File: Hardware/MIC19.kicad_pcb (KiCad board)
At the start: 2 copper layers, 85 parts, among them J1 Screw_Terminal_01x02, J2 Screw_Terminal_01x03, J401 USART, J601 RJ45, J602 RJ45, K1 coil: 12VDC, contact: 125V/10A, Q1 Q_NPN_BEC, U1 4N25, U201 MCP2551-I/SN, U202 MCP2515-xSO, U401 ATMEGA328P-PU, U501 LM7805, Y201 16MHz, Y401 16MHz

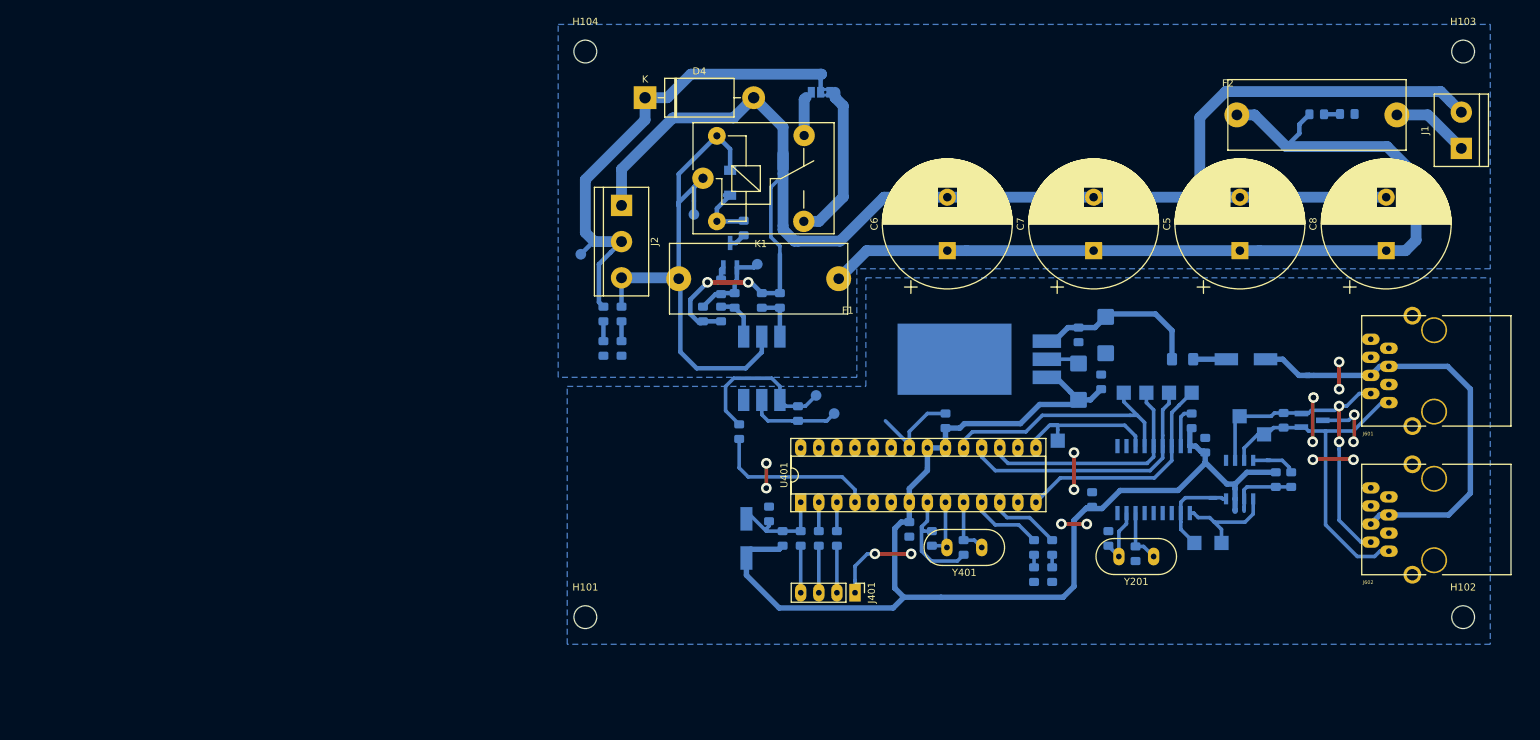
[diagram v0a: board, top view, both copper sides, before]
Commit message: Atualização do MIC19
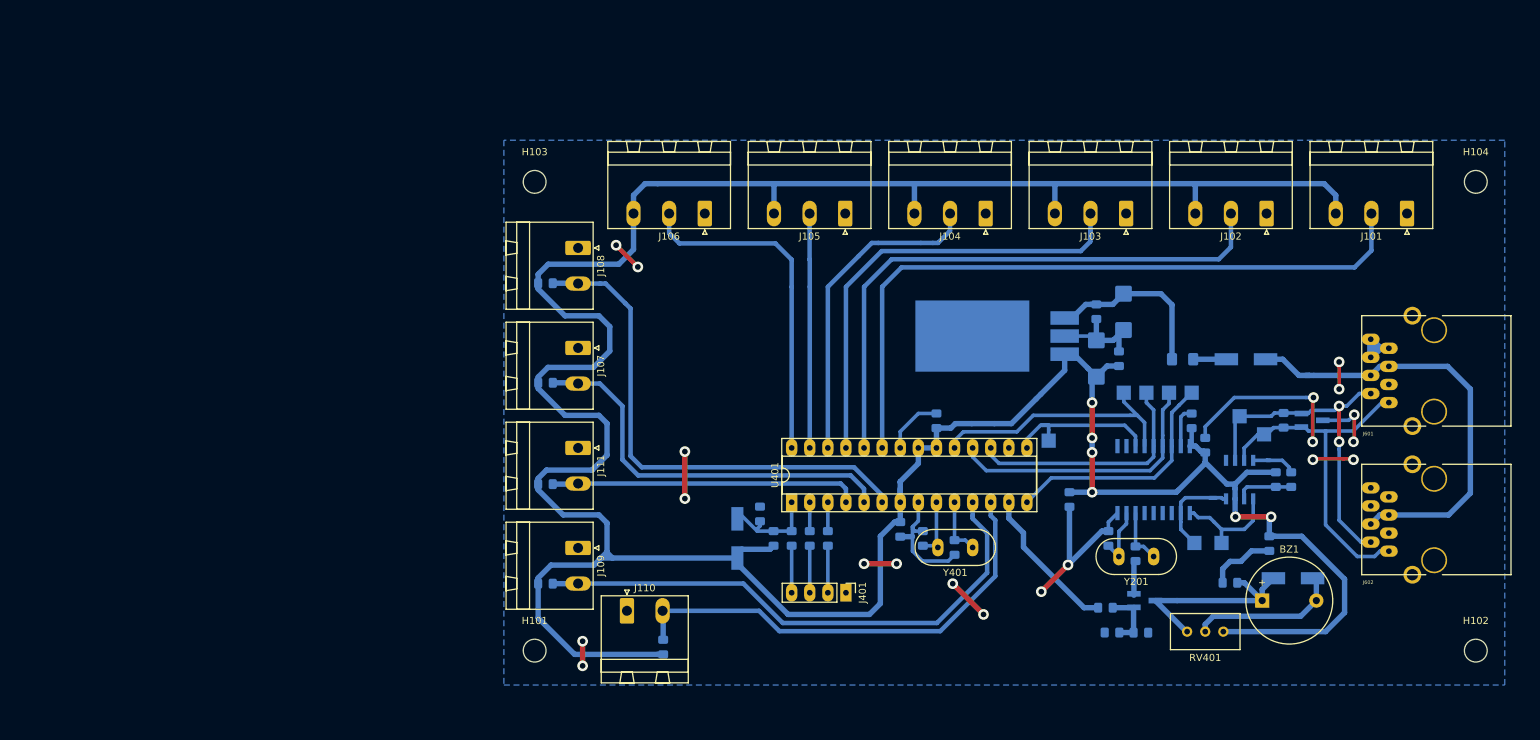
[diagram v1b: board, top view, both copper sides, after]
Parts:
- removed C1, C3, C4: 100n, Capacitor_SMD:C_0805_2012Metric_Pad1.15x1.40mm_HandSolder
- removed C2: 1n, Capacitor_SMD:C_0805_2012Metric_Pad1.15x1.40mm_HandSolder
- removed C5, C6, C7, C8: 4700u 35V, Capacitor_THT:CP_Radial_D18.0mm_P7.50mm
- removed D1, D5: G3mm, LED_SMD:LED_0805_2012Metric_Pad1.15x1.40mm_HandSolder
- removed D2: LL4148, Diode_SMD:D_MiniMELF
- removed D3: R3mm, LED_SMD:LED_0805_2012Metric_Pad1.15x1.40mm_HandSolder
- removed D4: MUR460, Diode_THT:D_DO-201AD_P15.24mm_Horizontal
- removed F1: 3A, KicadZeniteSolarLibrary18:Fuse_Holder_5x20
- removed F2: 10A, KicadZeniteSolarLibrary18:Fuse_Holder_5x20
- removed J1: Screw_Terminal_01x02, TerminalBlock:TerminalBlock_bornier-2_P5.08mm
- removed J2: Screw_Terminal_01x03, TerminalBlock:TerminalBlock_bornier-3_P5.08mm
- removed JP1: SolderJumper_3_Bridged12, Jumper:SolderJumper-3_P1.3mm_Bridged2Bar12_Pad1.0x1.5mm_NumberLabels
- removed K1: coil: 12VDC, contact: 125V/10A, Relay_THT:Relay_SPDT_SANYOU_SRD_Series_Form_C
- removed Q1: Q_NPN_BEC, Package_TO_SOT_SMD:TSOT-23_HandSoldering
- removed R1: 330R, Resistor_SMD:R_0805_2012Metric_Pad1.15x1.40mm_HandSolder
- removed R2: NC, Resistor_SMD:R_0805_2012Metric_Pad1.15x1.40mm_HandSolder
- removed R3: 1k2, Resistor_SMD:R_0805_2012Metric_Pad1.15x1.40mm_HandSolder
- removed R4, R7, R8: 1k, Resistor_SMD:R_0805_2012Metric_Pad1.15x1.40mm_HandSolder
- removed R5: 10k, Resistor_SMD:R_0805_2012Metric_Pad1.15x1.40mm_HandSolder
- removed R6: 120R, Resistor_SMD:R_0805_2012Metric_Pad1.15x1.40mm_HandSolder
- removed TP1: A1, TestPoint:TestPoint_Pad_D1.5mm
- removed TP2: K1, TestPoint:TestPoint_Pad_D1.5mm
- removed TP3: 12V, TestPoint:TestPoint_Pad_D1.5mm
- removed TP4: B1, TestPoint:TestPoint_Pad_D1.5mm
- removed TP5: OUT1, TestPoint:TestPoint_Pad_D1.5mm
- removed U1: 4N25, Package_DIP:DIP-6_W8.89mm_SMDSocket_LongPads
- added BZ1: Buzzer, Buzzer_Beeper:Buzzer_12x9.5RM7.6, F.Cu at (175.0, 121.5)
- added C407: 100nF, Capacitor_SMD:C_0805_2012Metric_Pad1.15x1.40mm_HandSolder, B.Cu at (158.0, 126.0)
- added J101: ENGINE_VEL, Connector_Phoenix_MSTB:PhoenixContact_MSTBA_2,5_3-G_1x03_P5.00mm_Horizontal, F.Cu at (195.3, 67.2)
- added J102: ENGINE_ACEL, Connector_Phoenix_MSTB:PhoenixContact_MSTBA_2,5_3-G_1x03_P5.00mm_Horizontal, F.Cu at (175.6, 67.2)
- added J103: MPPT_POT, Connector_Phoenix_MSTB:PhoenixContact_MSTBA_2,5_3-G_1x03_P5.00mm_Horizontal, F.Cu at (155.9, 67.2)
- added J104: SW_PUMP1_ON, Connector_Phoenix_MSTB:PhoenixContact_MSTBA_2,5_3-G_1x03_P5.00mm_Horizontal, F.Cu at (136.2, 67.2)
- added J105: SW_PUMP2_ON, Connector_Phoenix_MSTB:PhoenixContact_MSTBA_2,5_3-G_1x03_P5.00mm_Horizontal, F.Cu at (116.5, 67.2)
- added J106: SW_PUMP3_ON, Connector_Phoenix_MSTB:PhoenixContact_MSTBA_2,5_3-G_1x03_P5.00mm_Horizontal, F.Cu at (96.8, 67.2)
- added J107: SW_BOAT_ON, Connector_Phoenix_MSTB:PhoenixContact_MSTBA_2,5_2-G_1x02_P5.00mm_Horizontal, F.Cu at (79.0, 86.0)
- added J108: SW_ENGINE_ON, Connector_Phoenix_MSTB:PhoenixContact_MSTBA_2,5_2-G_1x02_P5.00mm_Horizontal, F.Cu at (79.0, 72.0)
- added J109: SW_MPPT_ON, Connector_Phoenix_MSTB:PhoenixContact_MSTBA_2,5_2-G_1x02_P5.00mm_Horizontal, F.Cu at (79.0, 114.1)
- added J110: SW_DMS, Connector_Phoenix_MSTB:PhoenixContact_MSTBA_2,5_2-G_1x02_P5.00mm_Horizontal, F.Cu at (85.9, 122.9)
- added J111: SW_EMERGENCIA, Connector_Phoenix_MSTB:PhoenixContact_MSTBA_2,5_2-G_1x02_P5.00mm_Horizontal, F.Cu at (79.0, 100.1)
- added Q101: BCV27, Package_TO_SOT_SMD:SOT-23_Handsoldering, B.Cu at (158.5, 121.5)
- added R101: 1k, Resistor_SMD:R_0805_2012Metric_Pad1.15x1.40mm_HandSolder, B.Cu at (74.4, 90.9)
- added R102: 1k, Resistor_SMD:R_0805_2012Metric_Pad1.15x1.40mm_HandSolder, B.Cu at (74.4, 77.0)
- added R103: 1k, Resistor_SMD:R_0805_2012Metric_Pad1.15x1.40mm_HandSolder, B.Cu at (74.4, 119.1)
- added R104: 1k, Resistor_SMD:R_0805_2012Metric_Pad1.15x1.40mm_HandSolder, B.Cu at (90.9, 128.0)
- added R105: 1k, Resistor_SMD:R_0805_2012Metric_Pad1.15x1.40mm_HandSolder, B.Cu at (74.4, 105.2)
- added R406: 330, Resistor_SMD:R_0805_2012Metric_Pad1.15x1.40mm_HandSolder, B.Cu at (176.0, 113.5)
- added RV401: 1K, Potentiometer_THT:Potentiometer_Bourns_3296W_Vertical, F.Cu at (164.5, 125.9)
- D402: value LED_RED -> BYD77; footprint LED_SMD:LED_0805_2012Metric_Pad1.15x1.40mm_HandSolder -> Diode_SMD:D_MiniMELF_Handsoldering
- R404, R405: value 1k -> 100R
- moved H103 131.6 mm to (72.9, 62.7)
- moved H104 126.3 mm to (205.0, 62.7)
- moved D402 33.8 mm to (179.3, 118.4), turned to 180 degrees
- moved D403 27.5 mm to (170.5, 119.0), turned to 180 degrees
- moved R405 16.2 mm to (153.9, 126.0), turned to 0 degrees
- moved R404 11.3 mm to (153.0, 122.5), turned to 0 degrees
- moved H101 8.52 mm to (72.9, 128.5)
- moved H102 5.02 mm to (205.0, 128.5)
- moved C501 4.10 mm to (155.5, 81.0)
- moved C502 4.10 mm to (151.7, 81.0)
- moved C503 4.10 mm to (154.9, 87.6)
- moved C504 4.10 mm to (151.7, 87.5)
- moved U501 4.10 mm to (146.0, 81.8)
- moved C201 3.17 mm to (148.0, 107.3), turned to 270 degrees
- moved C401 1.27 mm to (129.3, 96.3)
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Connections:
- D402 pad 1: GND -> Net-(BZ1-Pad2)
- D402 pad 2: Net-(D402-Pad2) -> Net-(BZ1-Pad1)
- D403 pad 1: GND -> Net-(BZ1-Pad1)
- R404 pad 1: /MCU/LED2 -> Net-(R404-Pad1)
- R404 pad 2: Net-(D402-Pad2) -> Net-(C407-Pad2)
- R405 pad 1: /MCU/LED1 -> GND
- R405 pad 2: Net-(D403-Pad2) -> Net-(C407-Pad2)
- U401 pad 11: /MCU/LED1 -> /Conectores/SW_MPPT_ON
- U401 pad 12: /MCU/LED2 -> /Conectores/SW_DMS
- U401 pad 13: Net-(U401-Pad13) -> Net-(R404-Pad1)
- U401 pad 23: Net-(U401-Pad23) -> /Conectores/ENGINE_VEL
- U401 pad 24: Net-(U401-Pad24) -> /Conectores/ENGINE_ACEL
- U401 pad 25: Net-(U401-Pad25) -> /Conectores/MPPT_POT
- U401 pad 26: Net-(U401-Pad26) -> /Conectores/SW_PUMP1_ON
- U401 pad 27: Net-(U401-Pad27) -> /Conectores/SW_PUMP2_ON
- U401 pad 28: Net-(U401-Pad28) -> /Conectores/SW_PUMP3_ON
- U401 pad 4: /MCU/ON_OFF_PUMP -> /Conectores/SW_EMERGENCIA
- U401 pad 5: Net-(U401-Pad5) -> /Conectores/SW_BOAT_ON
- U401 pad 6: Net-(U401-Pad6) -> /Conectores/SW_ENGINE_ON
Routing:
- net +5V: track 170.6 -> 475.8 mm, vias 0 -> 6
- net GNDPWR: track 239.1 -> 0.00 mm, vias 2 -> 0
- net +12V: track 126.9 -> 0.00 mm
- net /Conectores/ENGINE_VEL: track 0.00 -> 98.6 mm
- net /Conectores/ENGINE_ACEL: track 0.00 -> 81.7 mm
- net /pump_driver/Level_sensor: track 77.1 -> 0.00 mm
- net /Conectores/SW_MPPT_ON: track 0.00 -> 76.9 mm
- net /Conectores/SW_ENGINE_ON: track 0.00 -> 72.1 mm
- net /pump_driver/+Pump: track 69.5 -> 0.00 mm
- net /Conectores/SW_DMS: track 0.00 -> 65.8 mm
- net /Conectores/MPPT_POT: track 0.00 -> 64.3 mm
- net /Conectores/SW_BOAT_ON: track 0.00 -> 57.4 mm
- net /Conectores/SW_PUMP3_ON: track 0.00 -> 48.7 mm
- net GND: track 108.8 -> 156.5 mm, vias 16 -> 20
- net /Conectores/SW_PUMP1_ON: track 0.00 -> 45.5 mm
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- removed copper zone on B.Cu, net GNDPWR

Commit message: Formato da placa modificado
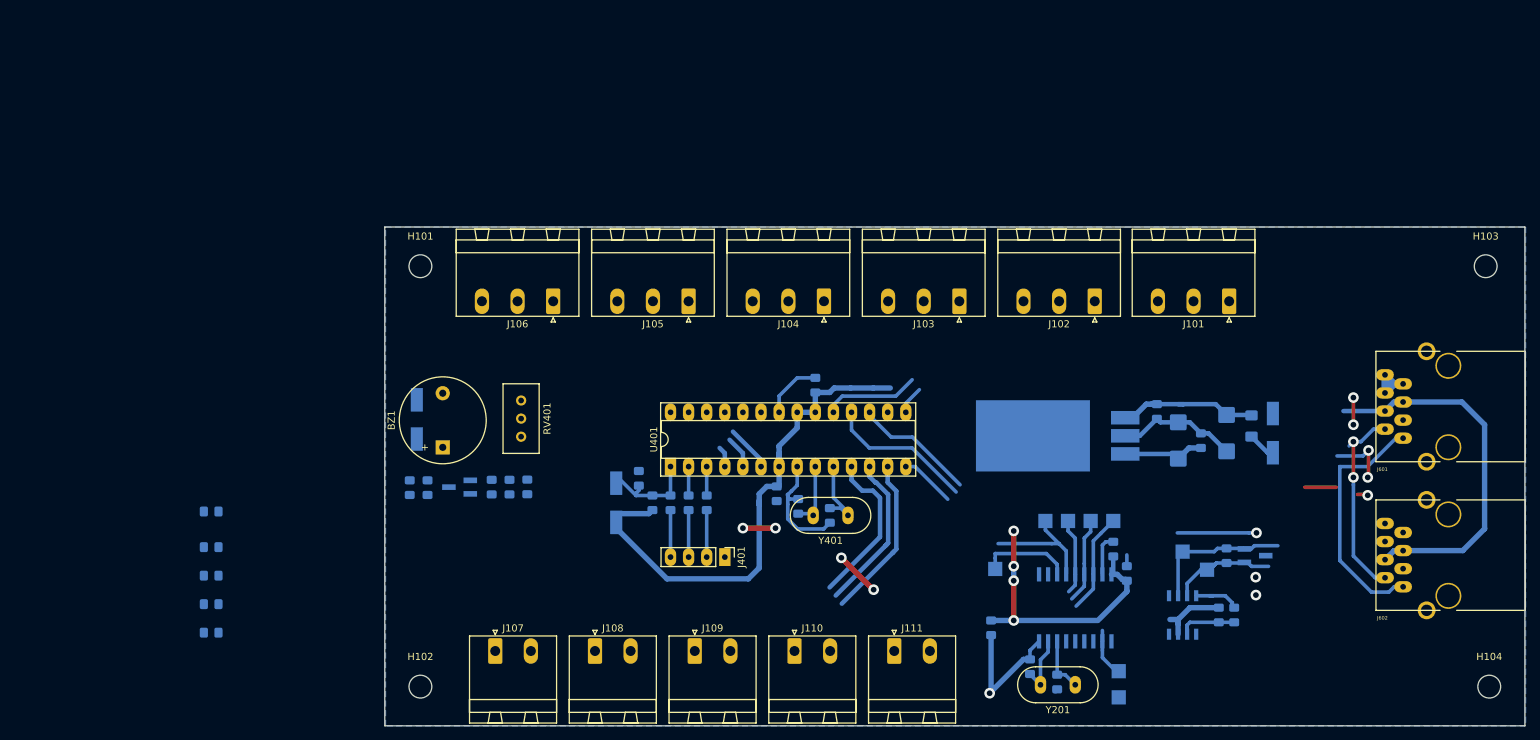
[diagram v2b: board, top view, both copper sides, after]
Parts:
- moved H102 148.2 mm to (56.9, 133.6)
- moved H103 134.0 mm to (206.4, 74.6)
- moved D402 125.0 mm to (56.4, 96.1), turned to 270 degrees
- moved R406 118.4 mm to (57.9, 105.7)
- moved BZ1 117.0 mm to (60.0, 100.0), turned to 90 degrees
- moved D403 115.9 mm to (55.4, 105.7), turned to 270 degrees
- moved Q101 97.4 mm to (62.4, 105.6), turned to 180 degrees
- moved RV401 97.4 mm to (71.0, 98.5), turned to 270 degrees
- moved C407 93.4 mm to (66.9, 105.6), turned to 90 degrees
- moved R405 87.0 mm to (69.4, 105.6), turned to 90 degrees
- moved R404 82.9 mm to (71.9, 105.6), turned to 90 degrees
- moved H104 70.9 mm to (206.9, 133.6)
- moved R104 66.2 mm to (27.5, 109.0), turned to 0 degrees
- moved R102 59.8 mm to (27.5, 114.0)
- moved J108 56.6 mm to (81.4, 128.6), turned to 0 degrees
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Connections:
- R404 pad 1: Net-(R404-Pad1) -> /MCU/BUZZER
- U201 pad 5: Net-(U201-Pad5) -> (no net)
- U202 pad 10: Net-(U202-Pad10) -> (no net)
- U202 pad 11: Net-(U202-Pad11) -> (no net)
- U202 pad 3: Net-(U202-Pad3) -> (no net)
- U202 pad 4: Net-(U202-Pad4) -> (no net)
- U202 pad 5: Net-(U202-Pad5) -> (no net)
- U202 pad 6: Net-(U202-Pad6) -> (no net)
- U401 pad 11: /Conectores/SW_MPPT_ON -> /Conectores/SW_BOAT_ON
- U401 pad 13: Net-(R404-Pad1) -> /Conectores/SW_EMERGENCIA
- U401 pad 16: Net-(U401-Pad16) -> (no net)
- U401 pad 4: /Conectores/SW_EMERGENCIA -> /Conectores/SW_MPPT_ON
- U401 pad 5: /Conectores/SW_BOAT_ON -> /Conectores/SW_ENGINE_ON
- U401 pad 6: /Conectores/SW_ENGINE_ON -> /MCU/BUZZER
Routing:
- net +5V: track 475.8 -> 137.9 mm, vias 6 -> 4
- net /Conectores/ENGINE_VEL: track 98.6 -> 0.00 mm
- net /Conectores/ENGINE_ACEL: track 81.7 -> 0.00 mm
- net /Conectores/SW_MPPT_ON: track 76.9 -> 2.92 mm
- net /Conectores/SW_ENGINE_ON: track 72.1 -> 4.99 mm
- net /Conectores/MPPT_POT: track 64.3 -> 0.00 mm
- net /Conectores/SW_PUMP3_ON: track 48.7 -> 0.00 mm
- net /Conectores/SW_PUMP1_ON: track 45.5 -> 0.00 mm
- net /Conectores/SW_DMS: track 65.8 -> 23.8 mm
- net GND: track 156.5 -> 122.0 mm, vias 20 -> 13
- net /Conectores/SW_BOAT_ON: track 57.4 -> 23.3 mm
- net /Conectores/SW_PUMP2_ON: track 32.9 -> 0.00 mm
- net Net-(BZ1-Pad1): track 29.6 -> 0.00 mm
- net Net-(BZ1-Pad2): track 21.8 -> 0.00 mm
- net Net-(R404-Pad1): track 21.2 -> 0.00 mm
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- added copper zone on B.Cu, net (none)
- removed copper zone on B.Cu, net GND
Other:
- board outline added: 160 x 70 mm
